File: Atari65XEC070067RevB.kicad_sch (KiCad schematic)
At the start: 341 parts, among them J1 SIO, J2 MONITOR, J5 JOY1, J6 JOY1, J7 DIN-7, J8 KEYBOARD, Q1 2N3904, Q2 2N3904, Q3 2N3904, Q4 2N3904, Q5 2N3904, Q6 2N3904, Q7 MPSA55, SW1 SW_SPDT, U1 LM358, U10 4164, U11 4164, U12 4164, U13 4164, U14 4164, U15 4164, U16 4164, U17 C014889/GTIA, U18 74LS08, U19 NE555P, U2 74LS138, U20 4050, U21 74LS74, U22 C012294/POKEY, U23 C014795 PIA/6520, U24 4051, U25 4051, U26 4164, U27 4164, U28 4164, U29 4164, U3 MMU, U30 4164, U31 4164, U32 4164, U33 4164, U34 MMMU, U35 74LS95, U4 BASIC, U5 OS ROM, U6 CO14806/SALLY, U7 C021698/ANTIC, U8 C061991/FREDDIE, U9 4164, Y2 4.33618MHz

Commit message: progress routing
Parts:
- C98: footprint Library:C_Axial_L5.1mm_D2.7mm_P12.72mm_Horizontal -> Capacitor_THT:CP_Axial_L11.0mm_D5.0mm_P18.00mm_Horizontal
- JA4: value ~ -> J4A; footprint (none) -> CARTRIDGE
- JB4: value EXPANSION -> J4B; footprint (none) -> Library:EXPANSION
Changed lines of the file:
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@@
 			)
 		)
-		(property "Value" "~"
-			(at 22.86 157.48 0)
+		(property "Value" "J4A"
+			(at 22.86 160.02 0)
 			(effects
 				(font
@@
 			)
 		)
-		(property "Footprint" ""
+		(property "Footprint" "CARTRIDGE"
 			(at 22.86 209.55 0)
 			(effects
@@
 			)
 		)
-		(property "Footprint" "Library:C_Axial_L5.1mm_D2.7mm_P12.72mm_Horizontal"
+		(property "Footprint" "Capacitor_THT:CP_Axial_L11.0mm_D5.0mm_P18.00mm_Horizontal"
 			(at 332.74 388.62 0)
 			(effects
@@
 			)
 		)
-		(property "Value" "EXPANSION"
+		(property "Value" "J4B"
 			(at 23.114 344.678 0)
 			(effects
@@
 			)
 		)
-		(property "Footprint" ""
+		(property "Footprint" "Library:EXPANSION"
 			(at 22.86 313.69 0)
 			(effects

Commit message: fix din ports
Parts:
- J7: footprint Library:CUI_SDS-70J -> Library:CUI_SDS-70J_Atari
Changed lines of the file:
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@@
 			)
 		)
-		(property "Footprint" "Library:CUI_SDS-70J"
+		(property "Footprint" "Library:CUI_SDS-70J_Atari"
 			(at 64.77 27.94 0)
 			(effects

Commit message: progress routing
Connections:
- net GND: now also C31.2
- net IRQ: no longer R21.1, U6.6 (~{NMI}), U7.7 (~{NMI})
- net REF: no longer C22.2, JB4.5 (AUD)
- net MPD: now reaches JB4.4 (~{MPD}), R15.2, U3.14 (~{MPD})
- net EXTSEL: now reaches JB4.1 (~{EXTSEL}), R30.2, U8.3 (EXTSEL)
- net RST: now reaches JB4.2 (~{RST}), U19.3 (Q), U23.34 (~{RESET}), U6.40 (~{RST}), U8.39 (~{RST})
- net D1xx: now reaches JB4.3 (~{D1XX}), U2.14 (O1)
- new net: R21.1, U6.6 (~{NMI}), U7.7 (~{NMI})
- new net AUD: C22.2, JB4.5 (AUD)
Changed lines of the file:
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@@
 	)
 	(junction
-		(at 198.12 151.13)
-		(diameter 0)
-		(color 0 0 0 0)
-	)
-	(junction
 		(at 142.24 22.86)
 		(diameter 0)
@@
 	)
 	(junction
-		(at 60.96 236.22)
-		(diameter 0)
-		(color 0 0 0 0)
-	)
-	(junction
 		(at 222.25 63.5)
 		(diameter 0)
@@
 	)
 	(junction
+		(at 226.06 205.74)
+		(diameter 0)
+		(color 0 0 0 0)
+	)
+	(junction
 		(at 355.6 384.81)
 		(diameter 0)
@@
 	(wire
 		(pts
-			(xy 198.12 151.13) (xy 203.2 151.13)
-		)
-		(stroke
-			(width 0)
-			(type default)
-		)
-	)
-	(wire
-		(pts
 			(xy 388.62 63.5) (xy 388.62 62.23)
 		)
@@
 	(wire
 		(pts
+			(xy 226.06 204.47) (xy 226.06 205.74)
+		)
+		(stroke
+			(width 0)
+			(type default)
+		)
+	)
+	(wire
+		(pts
 			(xy 426.72 194.31) (xy 426.72 233.68)
 		)
@@
 	(wire
 		(pts
-			(xy 48.26 236.22) (xy 60.96 236.22)
+			(xy 48.26 236.22) (xy 77.47 236.22)
 		)
 		(stroke
@@
 	(wire
 		(pts
-			(xy 185.42 151.13) (xy 198.12 151.13)
+			(xy 185.42 151.13) (xy 203.2 151.13)
 		)
 		(stroke
@@
 	(wire
 		(pts
-			(xy 198.12 153.67) (xy 198.12 151.13)
+			(xy 198.12 146.05) (xy 198.12 153.67)
 		)
 		(stroke
@@
 	(wire
 		(pts
-			(xy 60.96 236.22) (xy 77.47 236.22)
-		)
-		(stroke
-			(width 0)
-			(type default)
-		)
-	)
-	(wire
-		(pts
 			(xy 417.83 308.61) (xy 417.83 306.07)
 		)
@@
 		)
 	)
-	(wire
-		(pts
-			(xy 198.12 146.05) (xy 198.12 151.13)
-		)
-		(stroke
-			(width 0)
-			(type default)
-		)
-	)
 	(bus
 		(pts
@@
 	(wire
 		(pts
-			(xy 60.96 236.22) (xy 60.96 292.1)
+			(xy 60.96 149.86) (xy 60.96 292.1)
 		)
 		(stroke
@@
 		)
 	)
-	(wire
-		(pts
-			(xy 60.96 149.86) (xy 60.96 236.22)
-		)
-		(stroke
-			(width 0)
-			(type default)
-		)
-	)
 	(bus
 		(pts
@@
 		)
 	)
+	(label "MPD"
+		(at 33.02 294.64 0)
+		(effects
+			(font
+				(size 1.27 1.27)
+			)
+			(justify left bottom)
+		)
+	)
 	(label "CLOCK_OUT"
 		(at 527.05 356.87 0)
@@
 		)
 	)
+	(label "RST"
+		(at 33.02 312.42 0)
+		(effects
+			(font
+				(size 1.27 1.27)
+			)
+			(justify left bottom)
+		)
+	)
 	(label "A8"
 		(at 130.81 133.35 0)
@@
 		)
 	)
+	(label "AUD"
+		(at 33.02 292.1 0)
+		(effects
+			(font
+				(size 1.27 1.27)
+			)
+			(justify left bottom)
+		)
+	)
 	(label "D0"
 		(at 247.65 259.08 0)
@@
 		)
 	)
+	(label "EXTSEL"
+		(at 39.37 337.82 0)
+		(effects
+			(font
+				(size 1.27 1.27)
+			)
+			(justify left bottom)
+		)
+	)
 	(label "D7"
 		(at 226.06 176.53 0)
@@
 		(effects
 			(font
+				(size 1.27 1.27)
+			)
+			(justify left bottom)
+		)
+	)
+	(label "D1xx"
+		(at 33.02 287.02 0)
+		(effects
+			(font

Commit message: progress routing
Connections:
- net GND: now also JA4.B (GND); no longer C79.2, JA4.8 (GND)
- net S4: now reaches JA4.1 (~{S4}), U3.19 (~{S4})
- net S5: now reaches JA4.12 (~{S5}), U3.12 (~{S5})
- net RD4: now reaches JA4.A (RD4), R13.2, U3.7 (RD4)
- net T3 renamed RD5
- new net Shield: C79.2
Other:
- note added: "Shown as Shield in schematics but routed to ground on board. Shield only present on rear of board"
- note removed: "Technically only bridged on top of board"
- moved on the sheet: C16, C25, U18E, U1C

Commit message: add sio port
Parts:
- C79: footprint Capacitor_THT:CP_Radial_D8.0mm_P5.00mm -> Capacitor_THT:CP_Axial_L11.0mm_D5.0mm_P18.00mm_Horizontal
- J1: footprint (none) -> Library:DSUB-13_Pins_Horizontal_P2.77x2.84mm_EdgePinOffset7.70mm_Housed_MountingHolesOffset9.12mm
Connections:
- net GND: now also C79.2
- net RD4: now also R14.2; no longer R13.2
- net RD5: now also R13.2; no longer R14.2
- net Shield: no longer C79.2
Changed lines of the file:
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@@
 	)
 	(junction
+		(at 55.88 246.38)
+		(diameter 0)
+		(color 0 0 0 0)
+	)
+	(junction
 		(at 483.87 354.33)
 		(diameter 0)
@@
 	)
 	(junction
-		(at 55.88 248.92)
-		(diameter 0)
-		(color 0 0 0 0)
-	)
-	(junction
 		(at 218.44 284.48)
 		(diameter 0)
@@
 	)
 	(junction
+		(at 66.04 248.92)
+		(diameter 0)
+		(color 0 0 0 0)
+	)
+	(junction
 		(at 228.6 151.13)
 		(diameter 0)
@@
 	)
 	(junction
-		(at 66.04 246.38)
-		(diameter 0)
-		(color 0 0 0 0)
-	)
-	(junction
 		(at 242.57 271.78)
 		(diameter 0)
@@
 	(wire
 		(pts
+			(xy 55.88 246.38) (xy 63.5 246.38)
+		)
+		(stroke
+			(width 0)
+			(type default)
+		)
+	)
+	(wire
+		(pts
 			(xy 543.56 283.21) (xy 543.56 344.17)
 		)
@@
 	(wire
 		(pts
-			(xy 66.04 246.38) (xy 66.04 254)
-		)
-		(stroke
-			(width 0)
-			(type default)
-		)
-	)
-	(wire
-		(pts
 			(xy 553.72 346.71) (xy 553.72 363.22)
 		)
@@
 	(wire
 		(pts
-			(xy 55.88 254) (xy 55.88 248.92)
-		)
-		(stroke
-			(width 0)
-			(type default)
-		)
-	)
-	(wire
-		(pts
 			(xy 535.94 265.43) (xy 535.94 275.59)
 		)
@@
 	(wire
 		(pts
-			(xy 30.48 248.92) (xy 55.88 248.92)
-		)
-		(stroke
-			(width 0)
-			(type default)
-		)
-	)
-	(wire
-		(pts
 			(xy 31.75 110.49) (xy 31.75 120.65)
 		)
@@
 	(wire
 		(pts
-			(xy 30.48 246.38) (xy 63.5 246.38)
+			(xy 30.48 246.38) (xy 55.88 246.38)
 		)
 		(stroke
@@
 	(wire
 		(pts
-			(xy 55.88 248.92) (xy 85.09 248.92)
+			(xy 30.48 248.92) (xy 66.04 248.92)
 		)
 		(stroke
@@
 		)
 	)
+	(wire
+		(pts
+			(xy 55.88 254) (xy 55.88 246.38)
+		)
+		(stroke
+			(width 0)
+			(type default)
+		)
+	)
 	(bus
 		(pts
@@
 	(wire
 		(pts
-			(xy 66.04 246.38) (xy 85.09 246.38)
-		)
-		(stroke
-			(width 0)
-			(type default)
-		)
-	)
-	(wire
-		(pts
 			(xy 340.36 246.38) (xy 340.36 326.39)
 		)
@@
 	(wire
 		(pts
+			(xy 66.04 248.92) (xy 85.09 248.92)
+		)
+		(stroke
+			(width 0)
+			(type default)
+		)
+	)
+	(wire
+		(pts
 			(xy 229.87 316.23) (xy 229.87 317.5)
 		)
@@
 	(wire
 		(pts
-			(xy 63.5 246.38) (xy 66.04 246.38)
+			(xy 63.5 246.38) (xy 85.09 246.38)
 		)
 		(stroke
@@
 	(wire
 		(pts
+			(xy 66.04 254) (xy 66.04 248.92)
+		)
+		(stroke
+			(width 0)
+			(type default)
+		)
+	)
+	(wire
+		(pts
 			(xy 278.13 309.88) (xy 285.75 309.88)
 		)
@@
 			)
 		)
-		(property "Footprint" "Capacitor_THT:CP_Radial_D8.0mm_P5.00mm"
+		(property "Footprint" "Capacitor_THT:CP_Axial_L11.0mm_D5.0mm_P18.00mm_Horizontal"
 			(at 486.41 110.49 0)
 			(effects
@@
 			)
 		)
-		(property "Footprint" ""
+		(property "Footprint" "Library:DSUB-13_Pins_Horizontal_P2.77x2.84mm_EdgePinOffset7.70mm_Housed_MountingHolesOffset9.12mm"
 			(at 558.8 370.84 0)
 			(effects
@@
 	(symbol
 		(lib_id "power:GNDPWR")
-		(at 486.41 113.03 0)
+		(at 491.49 113.03 0)
 		(unit 1)
 		(exclude_from_sim no)
@@
 		(fields_autoplaced yes)
 		(property "Reference" "#PWR0173"
-			(at 486.41 118.11 0)
+			(at 491.49 118.11 0)
 			(effects
 				(font
@@
 		)
 		(property "Value" "Shield"
-			(at 486.283 116.84 0)
+			(at 491.363 116.84 0)
 			(effects
 				(font
@@
 		)
 		(property "Footprint" ""
-			(at 486.41 114.3 0)
+			(at 491.49 114.3 0)
 			(effects
 				(font
@@
 		)
 		(property "Datasheet" ""
-			(at 486.41 114.3 0)
+			(at 491.49 114.3 0)
 			(effects
 				(font
@@
 		)
 		(property "Description" "Power symbol creates a global label with name \"GNDPWR\" , global ground"
-			(at 486.41 113.03 0)
+			(at 491.49 113.03 0)
 			(effects
 				(font
@@
 					(unit 1)
 				)
+			)
+		)
+	)
+	(symbol
+		(lib_id "power:GND")
+		(at 486.41 113.03 0)
+		(unit 1)
+		(exclude_from_sim no)
+		(in_bom yes)
+		(on_board yes)
+		(dnp no)
+		(fields_autoplaced yes)
+		(property "Reference" "#PWR0180"
+			(at 486.41 119.38 0)
+			(effects
+				(font
+					(size 1.27 1.27)
+				)
+				(hide yes)
+			)
+		)
+		(property "Value" "GND"
+			(at 486.41 118.11 0)
+			(effects
+				(font
+					(size 1.27 1.27)
+				)
+				(hide yes)
+			)
+		)
+		(property "Footprint" ""
+			(at 486.41 113.03 0)
+			(effects
+				(font
+					(size 1.27 1.27)
+				)
+				(hide yes)
+			)
+		)
+		(property "Datasheet" ""
+			(at 486.41 113.03 0)
+			(effects
+				(font
+					(size 1.27 1.27)
+				)
+				(hide yes)
+			)
+		)
+		(property "Description" "Power symbol creates a global label with name \"GND\" , ground"
+			(at 486.41 113.03 0)
+			(effects
+				(font
+					(size 1.27 1.27)
+				)
+				(hide yes)
+			)
+		)
+		(pin "1"
+		)
+		(instances
+			(project "Atari65XEC070067RevB"
+				(path "/87d66ada-8337-4a7e-bc00-d889029d79b8"
+					(reference "#PWR0180")
+					(unit 1)
+				)

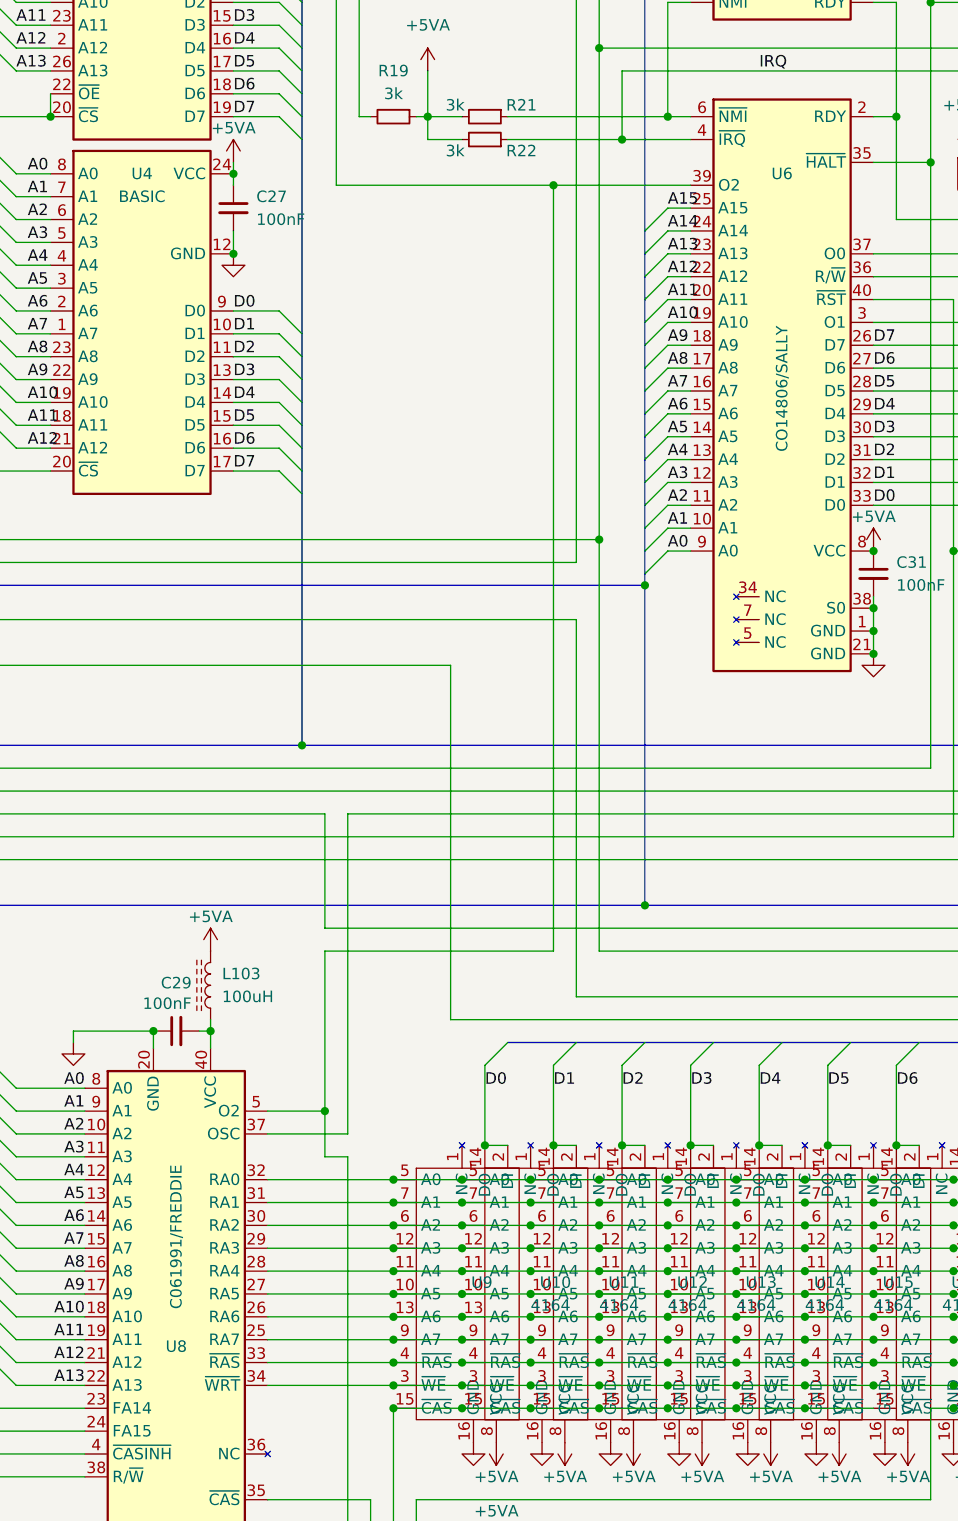
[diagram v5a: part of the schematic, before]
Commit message: fix numbering for U6 and U8 (swapped), more routing
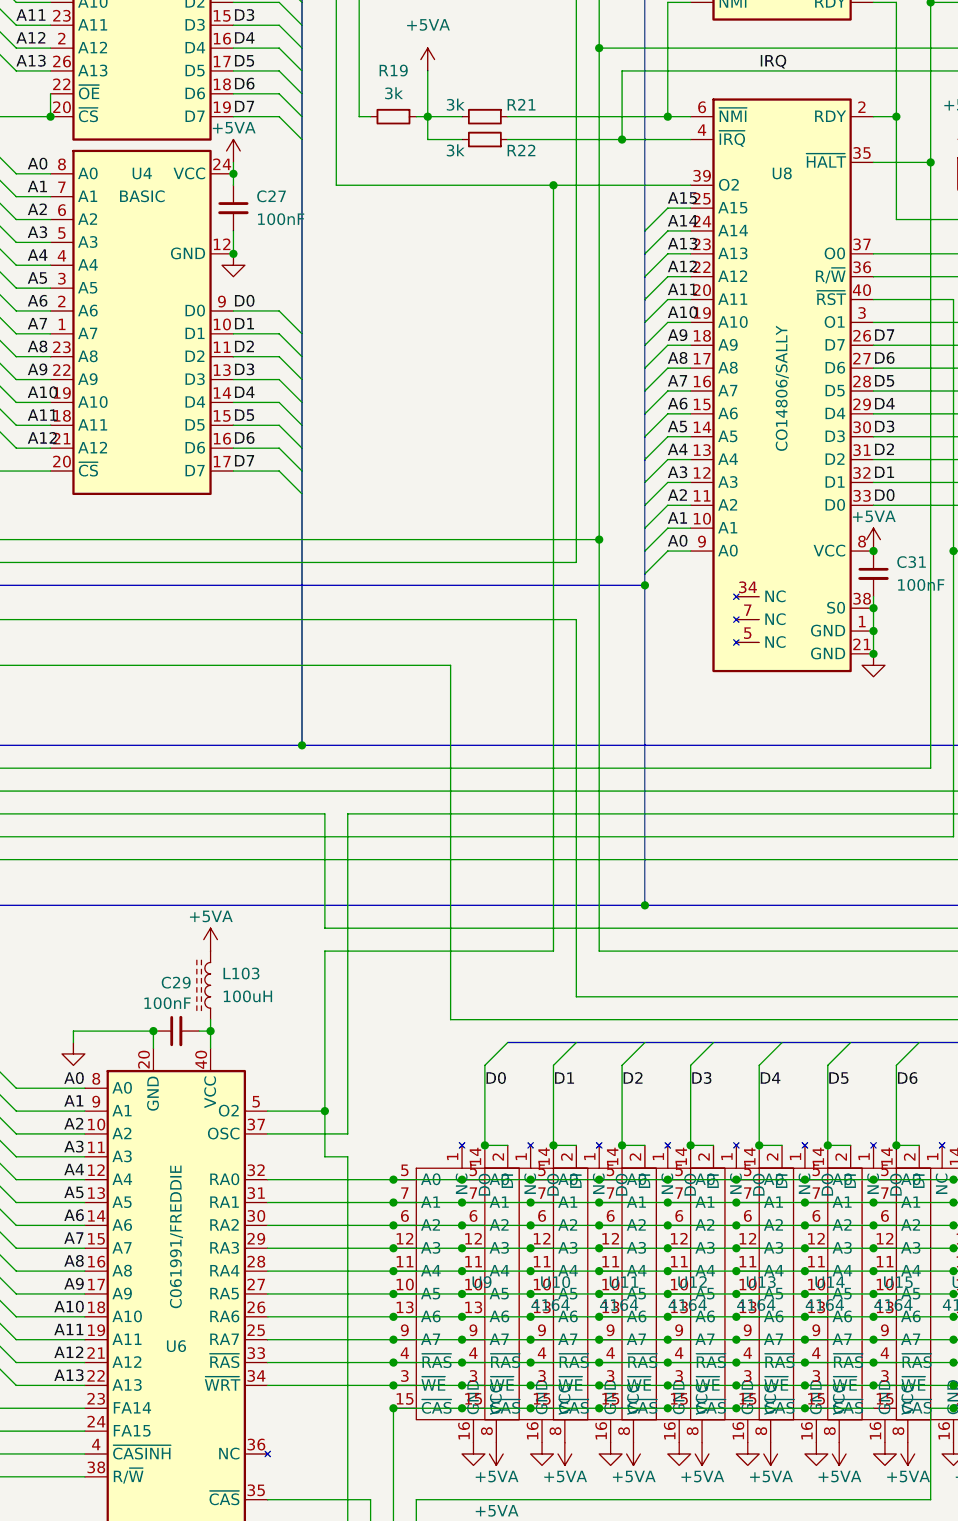
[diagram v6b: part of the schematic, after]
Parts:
- renumbered U8 to U6, U6 to U8
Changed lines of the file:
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@@
 		(on_board yes)
 		(dnp no)
-		(property "Reference" "U6"
+		(property "Reference" "U8"
 			(at 215.9 157.48 0)
 			(effects
@@
 			(project ""
 				(path "/87d66ada-8337-4a7e-bc00-d889029d79b8"
-					(reference "U6")
+					(reference "U8")
 					(unit 1)
 				)
@@
 		(on_board yes)
 		(dnp no)
-		(property "Reference" "U8"
+		(property "Reference" "U6"
 			(at 148.59 287.782 0)
 			(effects
@@
 			(project ""
 				(path "/87d66ada-8337-4a7e-bc00-d889029d79b8"
-					(reference "U8")
+					(reference "U6")
 					(unit 1)
 				)

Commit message: finish component placing
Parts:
- C99, L101, L24: now not fitted
- renumbered C25 to C43
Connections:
- net +5VD: now also J5.7, J6.7
- net A0: now also U23.35 (A0); no longer U23.36 (A0)
- net A1: now also U23.36 (A1); no longer U23.35 (A1)
- net CLOCK_IN: now also C301.2; no longer C302.2
- net CLOCK_OUT: now also C302.2; no longer C301.2
- net GND: now also J5.8, J6.8; no longer C305.2, C307.2, C310.2, C82.1, C83.1, C84.1, J1.13, J1.7, J1.9, R117.2, R118.2, R119.2
- net at R118.1, U23.18 (CB1): no longer R93.1
- new net COMMAND: C305.2, C84.1, J1.7, R119.2
- new net INTERRUPT: C310.2, C83.1, J1.13, R118.2, R93.1
- new net PROCEED: C307.2, C82.1, J1.9, R117.2
- now unconnected: L101.2, L24.1
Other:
- moved on the sheet: R117, R118, R92, R93, R94
